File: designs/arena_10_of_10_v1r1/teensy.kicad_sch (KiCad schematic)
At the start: 35 parts, among them U1 Teensy4.1

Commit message: Worked on ethernet.
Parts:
- removed U1: Teensy4.1, teensy:Teensy41_outer_only, symbol arena_custom:Teensy4.1
- added J?: Cetus RJ45 Magjack, symbol Cetus_RJ45_MagJack:Cetus_RJ45_Magjack
- added U?: Teensy4.1, symbol teensy:Teensy4.1_Ethernet_only
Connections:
- net +3.3V: now also U?.15 (3V3), U?.46 (3V3)
- net AIN.A0: now also U?.36 (14_A0_TX3_SPDIF_OUT)
- net AIN.A1: now also U?.37 (15_A1_RX3_SPDIF_IN)
- net GND: now also U?.1 (GND), U?.34 (GND), U?.47 (GND)
- net SCL: now also U?.41 (19_A5_SCL)
- net SDA: now also U?.40 (18_A4_SDA)
- net TNY.MISO_B0: now also U?.14 (12_MISO_MQSL)
- net TNY.MISO_B1: now also U?.3 (1_TX1_CTX2_MISO1)
- net at R?.2: now also U?.45 (23_A9_CRX1_MCLK1)
- net at R?.2: now also U?.4 (2_OUT2)
- net at J?.1 (Pin_1): now also U?.48 (VIN)
- net at R?.2: now also U?.5 (3_LRCLK2)
- net at R?.2: now also U?.12 (10_CS_MQSR)
- net at R?.2: now also U?.23 (31_CTX3)
- net at R?.2: now also U?.43 (21_A7_RX5_BCLK1)
- net at R?.2: now also U?.44 (22_A8_CTX1)
- net at R?.2: now also U?.20 (28_RX7)
- net at U?.2 (A): now also U?.28 (36_CS)
- net at R?.2: now also U?.10 (8_TX2_IN1)
- net at R?.2: now also U?.11 (9_OUT1C)
- net at R?.2: now also U?.13 (11_MOSI_CTX1)
- net at R?.2: now also U?.16 (24_A10_TX6_SCL2)
- net at R?.2: now also U?.17 (25_A11_RX6_SDA2)
- net at R?.2: now also U?.18 (26_A12_MOSI1)
- net at R?.2: now also U?.19 (27_A13_SCK1)
- net at R?.2: now also U?.2 (0_RX1_CRX2_CS1)
- net at R?.2: now also U?.21 (29_TX7)
- net at R?.2: now also U?.22 (30_CRX3)
- net at R?.2: now also U?.24 (32_OUT1B)
- net at R?.2: now also U?.25 (33_MCLK2)
- net at U?.2 (A): now also U?.29 (37_CS)
- net at R?.2: now also U?.35 (13_SCK_LED)
- net at R?.2: now also U?.6 (4_BCLK2)
- net at R?.2: now also U?.7 (5_IN2)
- net at R?.2: now also U?.8 (6_OUT1D)
- net at R?.2: now also U?.9 (7_RX2_OUT1A)
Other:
- note removed: "To do 1. Add external ethernet"
- moved on the sheet: C?, J?, R?, U?

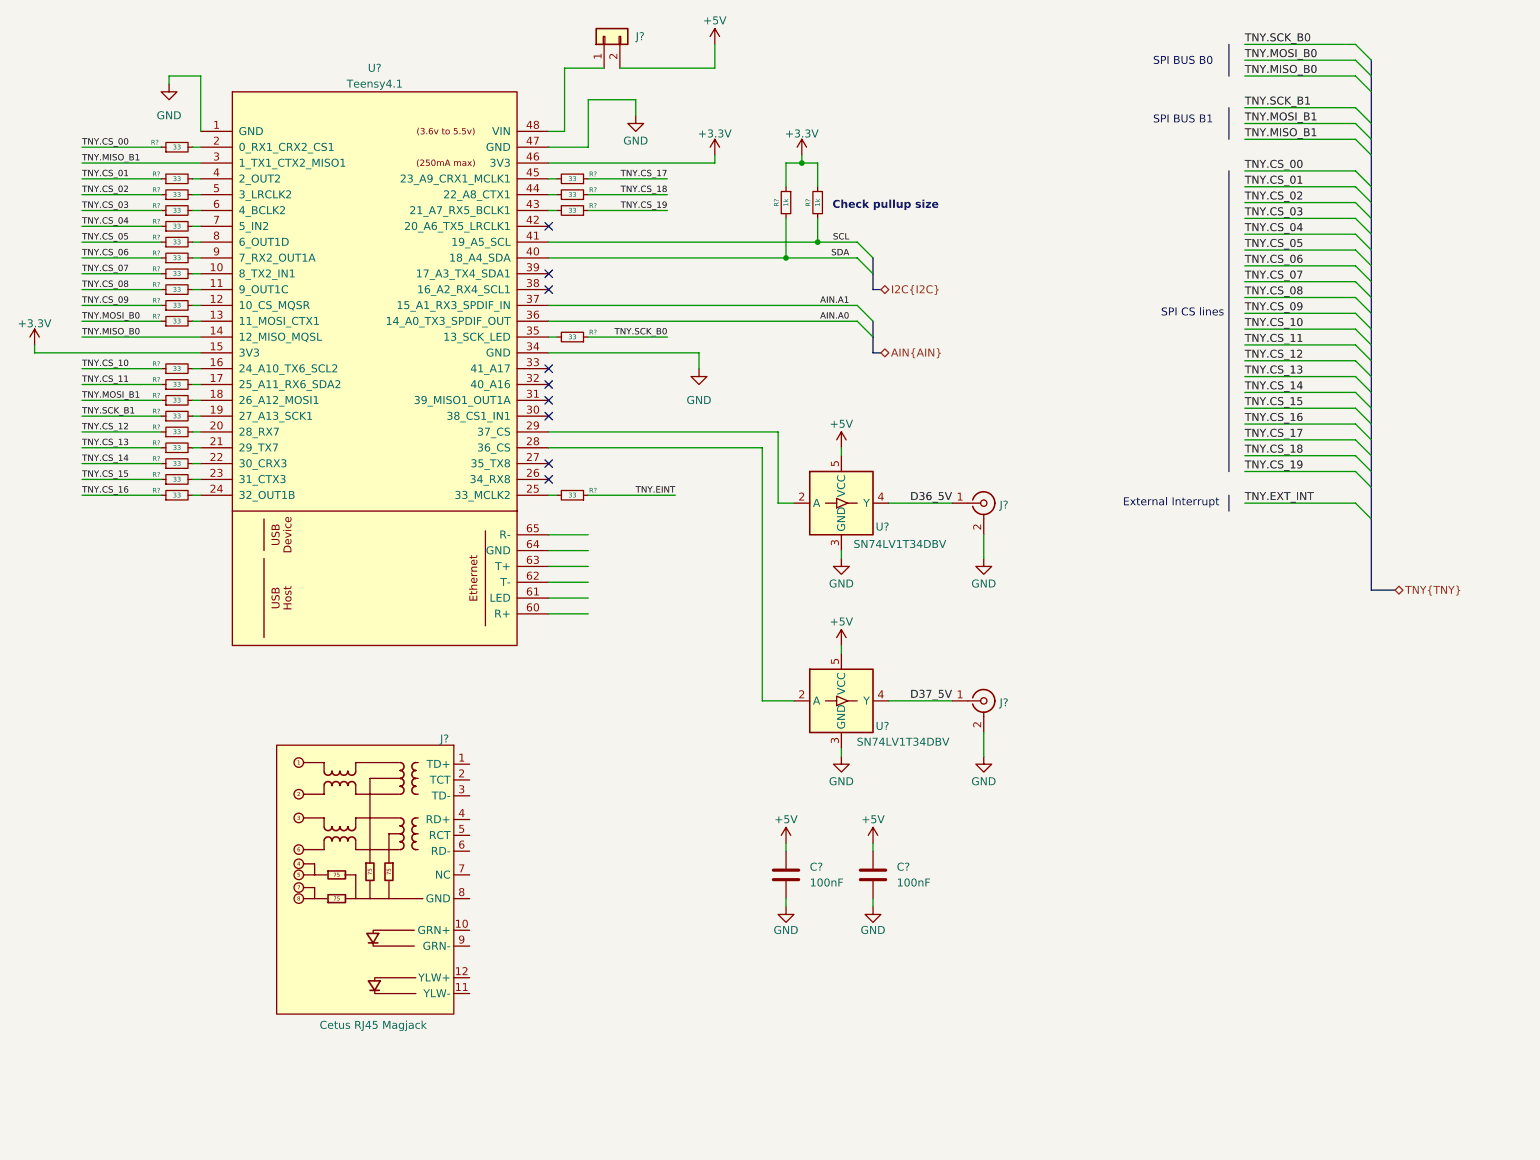
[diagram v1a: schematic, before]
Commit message: Fixed some issues with analog subsystem and added ethernet connection.
Added +/-15V power rails for bipolar analog inputs. Added 10V reference
voltage. Fixed connections for ethernet connection to teensy.
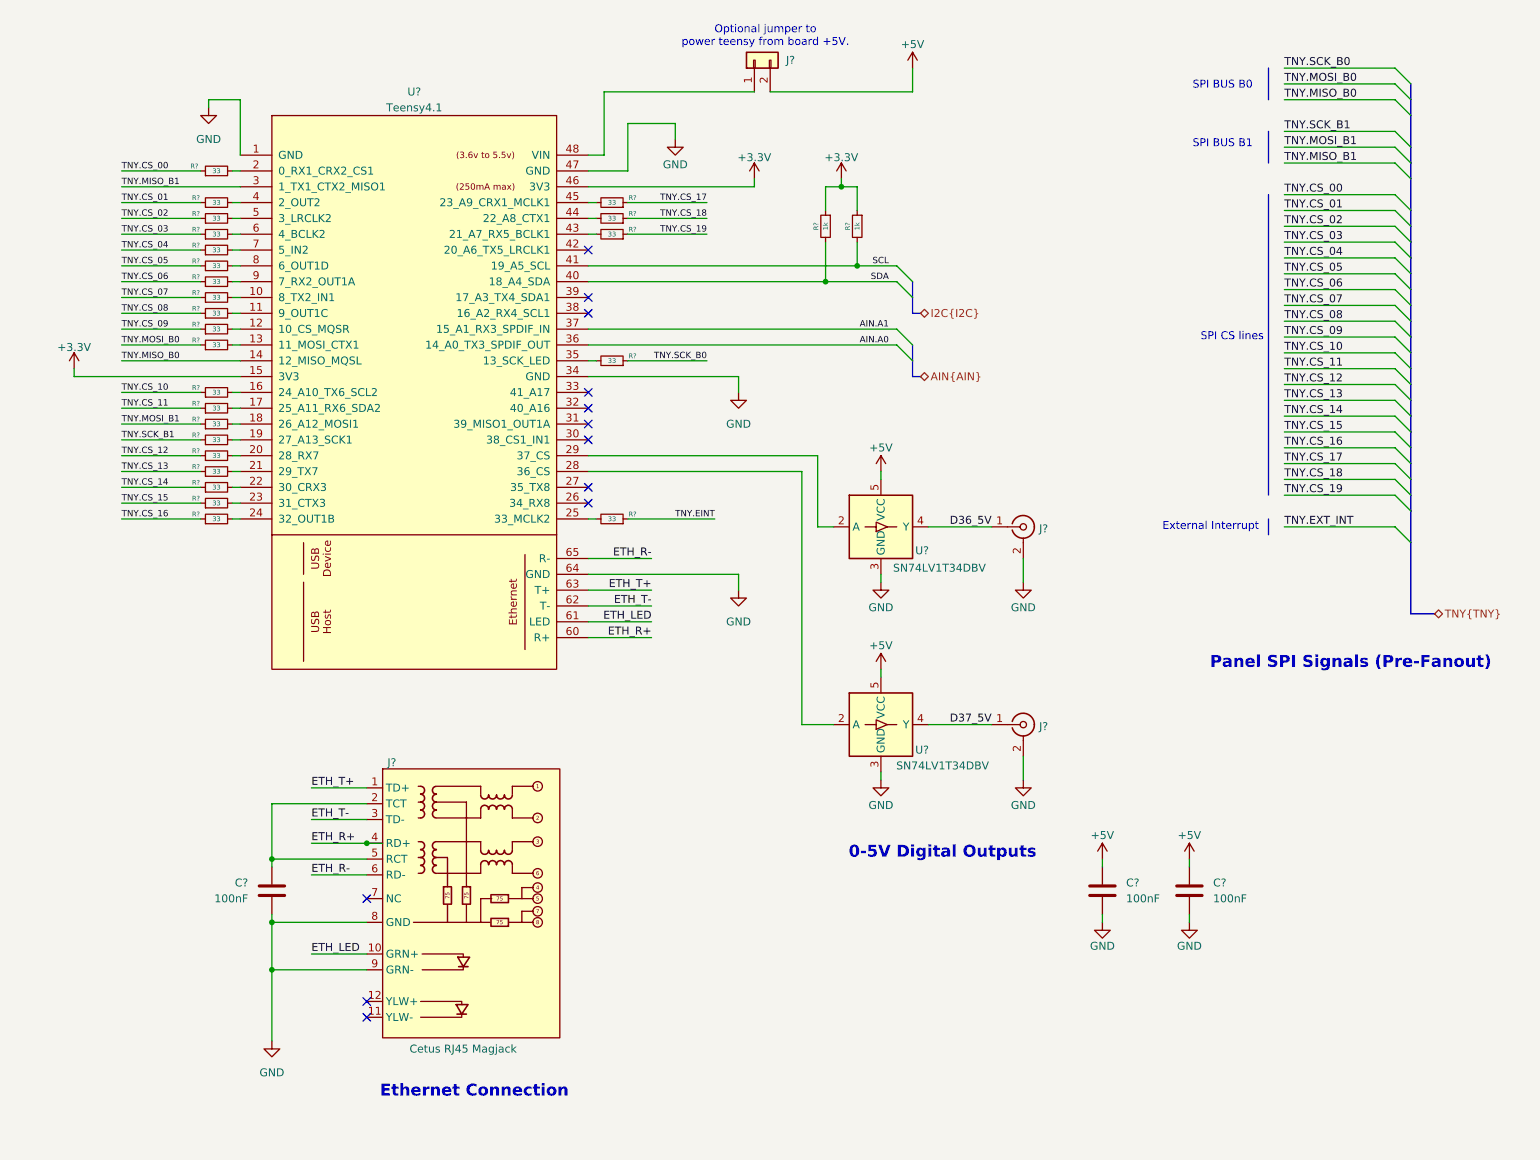
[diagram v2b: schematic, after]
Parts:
- added C?: 100nF, Capacitor_SMD:C_0402_1005Metric, symbol Device:C
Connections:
- net GND: now also J?.8 (GND), J?.9 (GRN-), U?.64 (GND), C?.2
- net ETH_R+: now reaches U?.60 (R+)
- net ETH_R+: now also J?.4 (RD+)
- net ETH_LED: now reaches U?.61 (LED)
- net ETH_LED: now also J?.10 (GRN+)
- net ETH_T-: now reaches U?.62 (T-)
- net ETH_T-: now also J?.3 (TD-)
- net ETH_T+: now reaches U?.63 (T+)
- net ETH_T+: now also J?.1 (TD+)
- net ETH_R-: now reaches U?.65 (R-)
- net ETH_R-: now also J?.6 (RD-)
- net at J?.2 (TCT): now also J?.5 (RCT), C?.1
- no-connect marks 9 -> 12
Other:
- note added: "0-5V Digital Outputs"
- note added: "Ethernet Connection"
- note added: "Optional jumper to power teensy from board +5V."
- note added: "Panel SPI Signals (Pre-Fanout)"
- note removed: "Check pullup size"
- moved on the sheet: C?, J?, R?, U?

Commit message: Added initial annotation.
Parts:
- gave numbers to parts that had none: 37

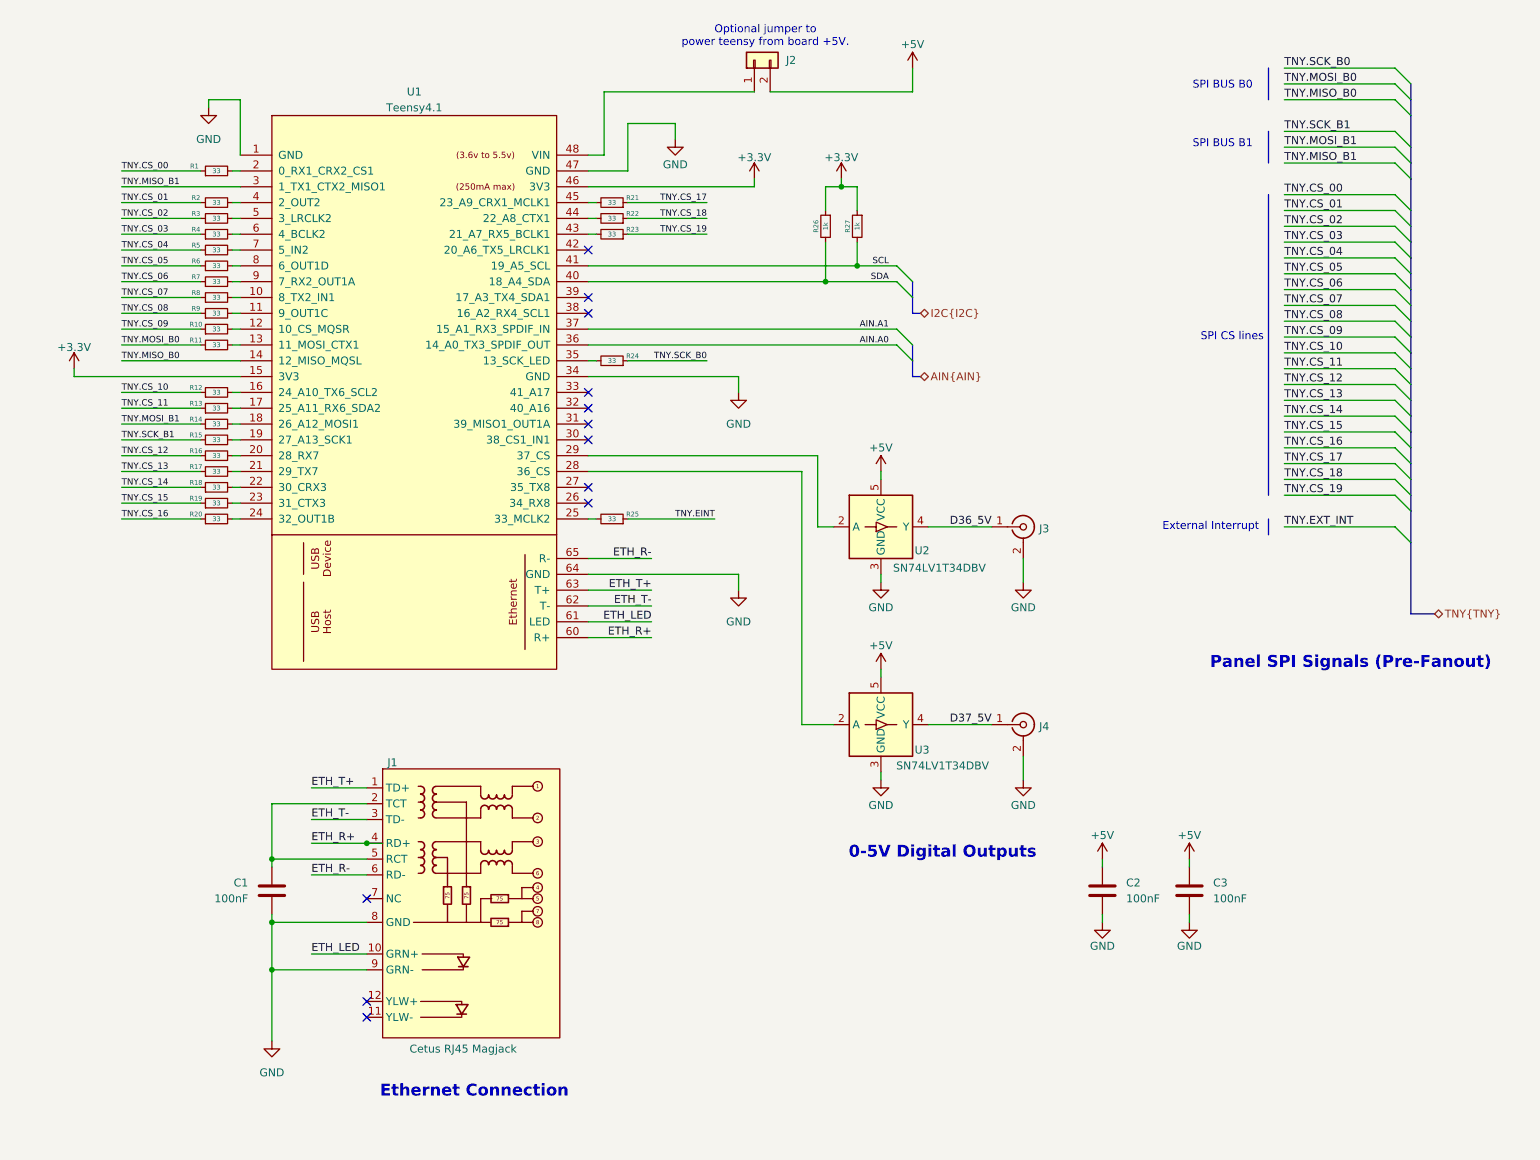
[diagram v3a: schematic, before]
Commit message: Finished footprint assignment.
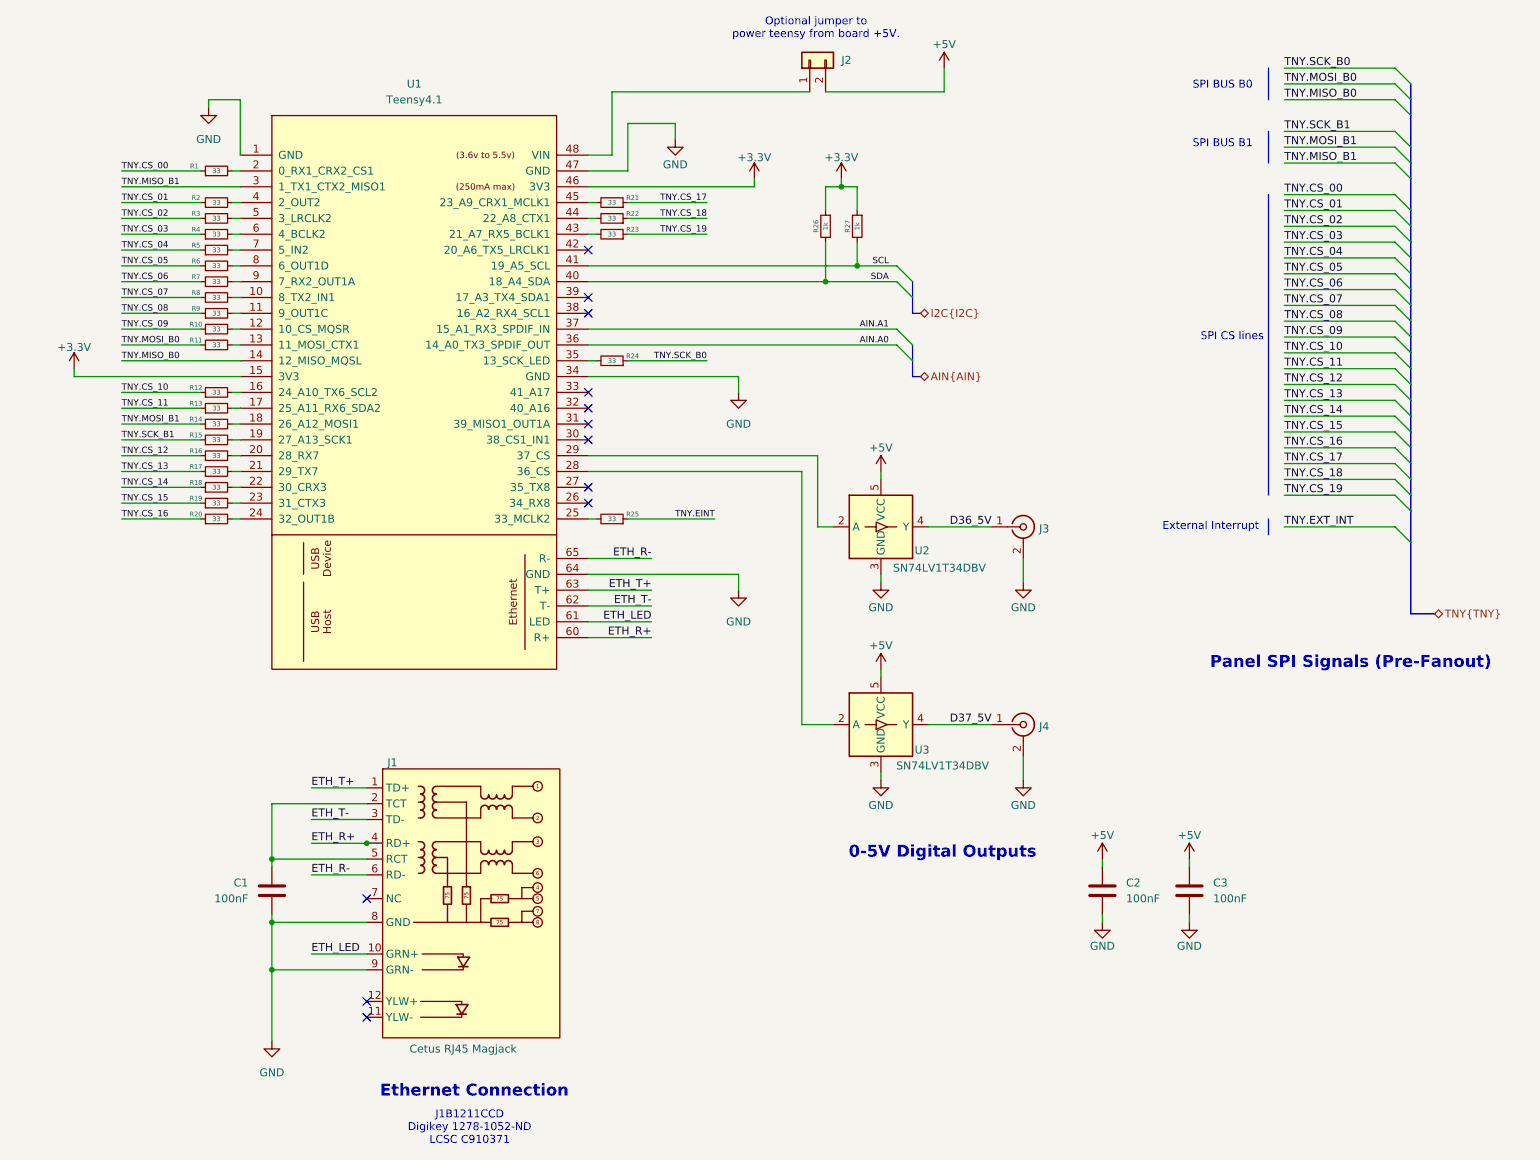
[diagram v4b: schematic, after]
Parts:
- removed U1: Teensy4.1, symbol teensy:Teensy4.1_Ethernet_only
- added U1: Teensy4.1, teensy:Teensy41_ethernet_only, symbol teensy:Teensy4.1_Ethernet_Only
- J1: footprint (none) -> Connector_RJ:RJ45_Cetus_J1B1211CCD_Horizontal
- J2: footprint (none) -> Connector_PinHeader_2.54mm:PinHeader_1x02_P2.54mm_Vertical
- J3, J4: footprint (none) -> BNC:BNC
- R1, R10, R11, R12, R13, R14, R15, R16, R17, R18, R19, R2, R20, R21, R22, R23, R24, R25, R26, R27, R3, R4, R5, R6, R7, R8, R9: footprint (none) -> Resistor_SMD:R_0402_1005Metric
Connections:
- net +3.3V: now also U1.15 (3V3), U1.46 (3V3)
- net AIN.A0: now also U1.36 (14_A0_TX3_SPDIF_OUT)
- net AIN.A1: now also U1.37 (15_A1_RX3_SPDIF_IN)
- net ETH_LED: now also U1.61 (LED)
- net ETH_R+: now also U1.60 (R+)
- net ETH_R-: now also U1.65 (R-)
- net ETH_T+: now also U1.63 (T+)
- net ETH_T-: now also U1.62 (T-)
- net GND: now also U1.1 (GND), U1.34 (GND), U1.47 (GND), U1.64 (GND)
- net SCL: now also U1.41 (19_A5_SCL)
- net SDA: now also U1.40 (18_A4_SDA)
- net TNY.MISO_B0: now also U1.14 (12_MISO_MQSL)
- net TNY.MISO_B1: now also U1.3 (1_TX1_CTX2_MISO1)
- net at R21.2: now also U1.45 (23_A9_CRX1_MCLK1)
- net at R2.2: now also U1.4 (2_OUT2)
- net at J2.1 (Pin_1): now also U1.48 (VIN)
- net at R3.2: now also U1.5 (3_LRCLK2)
- net at R10.2: now also U1.12 (10_CS_MQSR)
- net at R19.2: now also U1.23 (31_CTX3)
- net at R23.2: now also U1.43 (21_A7_RX5_BCLK1)
- net at R22.2: now also U1.44 (22_A8_CTX1)
- net at R8.2: now also U1.10 (8_TX2_IN1)
- net at R9.2: now also U1.11 (9_OUT1C)
- net at R11.2: now also U1.13 (11_MOSI_CTX1)
- net at R12.2: now also U1.16 (24_A10_TX6_SCL2)
- net at R13.2: now also U1.17 (25_A11_RX6_SDA2)
- net at R14.2: now also U1.18 (26_A12_MOSI1)
- net at R15.2: now also U1.19 (27_A13_SCK1)
- net at R1.2: now also U1.2 (0_RX1_CRX2_CS1)
- net at R16.2: now also U1.20 (28_RX7)
- net at R17.2: now also U1.21 (29_TX7)
- net at R18.2: now also U1.22 (30_CRX3)
- net at R20.2: now also U1.24 (32_OUT1B)
- net at R25.2: now also U1.25 (33_MCLK2)
- net at U3.2 (A): now also U1.28 (36_CS)
- net at U2.2 (A): now also U1.29 (37_CS)
- net at R24.2: now also U1.35 (13_SCK_LED)
- net at R4.2: now also U1.6 (4_BCLK2)
- net at R5.2: now also U1.7 (5_IN2)
- net at R6.2: now also U1.8 (6_OUT1D)
- net at R7.2: now also U1.9 (7_RX2_OUT1A)
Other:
- note added: "J1B1211CCD Digikey 1278-1052-ND LCSC C910371"
- moved on the sheet: J2
